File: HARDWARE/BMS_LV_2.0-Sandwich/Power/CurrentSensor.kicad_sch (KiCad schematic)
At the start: 7 parts, among them U5 ACHS-7123

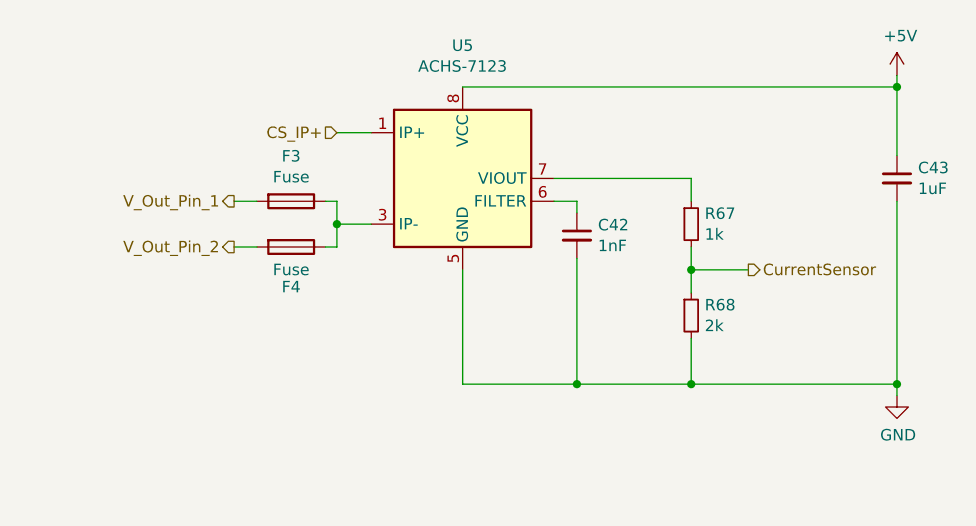
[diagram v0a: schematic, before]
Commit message: Zmieniono polozenie bezpiecznikow, dodano ledy sygnalizujące czy bezpiecznik jest cały
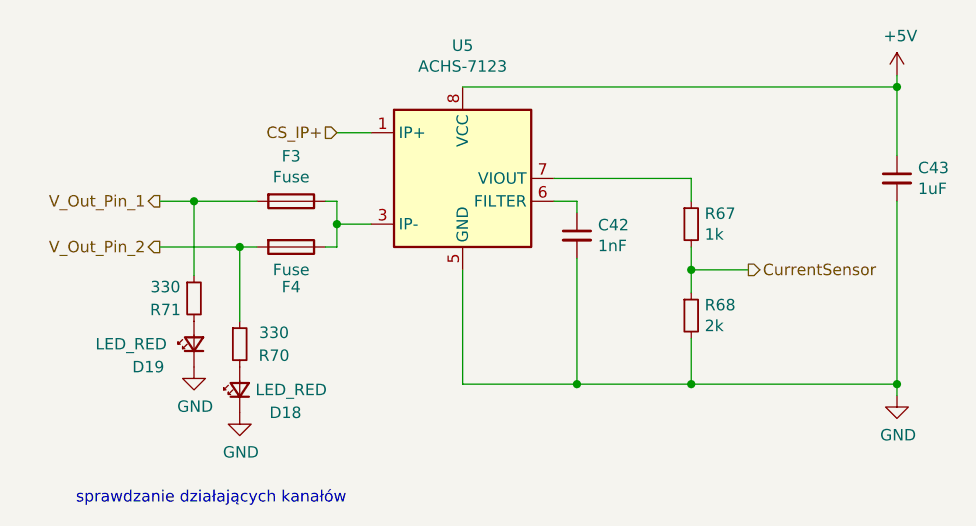
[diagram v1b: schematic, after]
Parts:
- added D18, D19: LED_RED, LED_SMD:LED_0603_1608Metric, symbol Device:LED_Small
- added R70, R71: 330, Resistor_SMD:R_0603_1608Metric, symbol Device:R_Small
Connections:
- net GND: now also D18.1 (K), D19.1 (K)
- net V_Out_Pin_1: now also R71.1
- net V_Out_Pin_2: now also R70.1
- new net: D19.2 (A), R71.2
- new net: D18.2 (A), R70.2
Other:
- note added: "sprawdzanie działających kanałów"

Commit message: sync
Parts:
- R70, R71: value 330 -> 1k5
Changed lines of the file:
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@@
 			)
 		)
-		(property "Value" "330"
+		(property "Value" "1k5"
 			(at 104.14 106.045 0)
 			(effects
@@
 			)
 		)
-		(property "Value" "330"
+		(property "Value" "1k5"
 			(at 116.205 111.125 0)
 			(effects

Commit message: Wersja obu plytek gotowa do sprawdzenia
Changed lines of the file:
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@@
+	)
+	(symbol
+		(lib_id "Device:Fuse")
+		(at 118.11 101.6 270)
+		(unit 1)
+		(exclude_from_sim no)
+		(in_bom yes)
+		(on_board yes)
+		(dnp no)
+		(property "Reference" "F4"
+			(at 118.11 96.5962 90)
+			(effects
+				(font
+					(size 1.27 1.27)
+				)
+			)
+		)
+		(property "Value" "Fuse"
+			(at 118.11 98.9076 90)
+			(effects
+				(font
+					(size 1.27 1.27)
+				)
+			)
+		)
+		(property "Footprint" "footprints:FUSC6125X279N"
+			(at 118.11 99.822 90)
+			(effects
+				(font
+					(size 1.27 1.27)
+				)
+				(hide yes)
+			)
+		)
+		(property "Datasheet" "https://www.mouser.pl/ProductDetail/Bel-Fuse/0680L9100-05?qs=XeJtXLiO41RjXNhvn3uPUw%3D%3D"
+			(at 118.11 101.6 0)
+			(effects
+				(font
+					(size 1.27 1.27)
+				)
+				(hide yes)
+			)
+		)
+		(property "Description" "500A interrupt fuse"
+			(at 118.11 101.6 0)
+			(effects
+				(font
+					(size 1.27 1.27)
+				)
+				(hide yes)
+			)
+		)
+		(property "Part Number" "0680L9100-05 "
+			(at 118.11 101.6 0)
+			(effects
+				(font
+					(size 1.27 1.27)
+				)
+				(hide yes)
+			)
+		)
+		(pin "2"
+		)
+		(pin "1"
+		)
+		(instances
+			(project "BMS_LV_2022"
+				(path "/fb6504b5-591d-4b10-ab86-0c46f59e8b7d/00000000-0000-0000-0000-000062c2dd72"
+					(reference "F4")
+					(unit 1)
+				)
+			)
+		)
 	)
 	(symbol
@@
 					(unit 1)
 				)
-			)
-		)
-	)
-	(symbol
-		(lib_id "Device:Fuse")
-		(at 118.11 101.6 270)
-		(unit 1)
-		(exclude_from_sim no)
-		(in_bom yes)
-		(on_board yes)
-		(dnp no)
-		(property "Reference" "F4"
-			(at 118.11 106.045 90)
-			(effects
-				(font
-					(size 1.27 1.27)
-				)
-			)
-		)
-		(property "Value" "Fuse"
-			(at 118.11 104.14 90)
-			(effects
-				(font
-					(size 1.27 1.27)
-				)
-			)
-		)
-		(property "Footprint" "footprints:FUSC6125X279N"
-			(at 118.11 99.822 90)
-			(effects
-				(font
-					(size 1.27 1.27)
-				)
-				(hide yes)
-			)
-		)
-		(property "Datasheet" "https://www.mouser.pl/ProductDetail/Bel-Fuse/0680L9100-05?qs=XeJtXLiO41RjXNhvn3uPUw%3D%3D"
-			(at 118.11 101.6 0)
-			(effects
-				(font
-					(size 1.27 1.27)
-				)
-				(hide yes)
-			)
-		)
-		(property "Description" "500A interrupt fuse"
-			(at 118.11 101.6 0)
-			(effects
-				(font
-					(size 1.27 1.27)
-				)
-				(hide yes)
-			)
-		)
-		(property "Part Number" "0680L9100-05 "
-			(at 118.11 101.6 0)
-			(effects
-				(font
-					(size 1.27 1.27)
-				)
-				(hide yes)
-			)
-		)
-		(pin "2"
-		)
-		(pin "1"
-		)
-		(instances
-			(project "BMS_LV_2022"
-				(path "/fb6504b5-591d-4b10-ab86-0c46f59e8b7d/00000000-0000-0000-0000-000062c2dd72"
-					(reference "F4")
-					(unit 1)
-				)

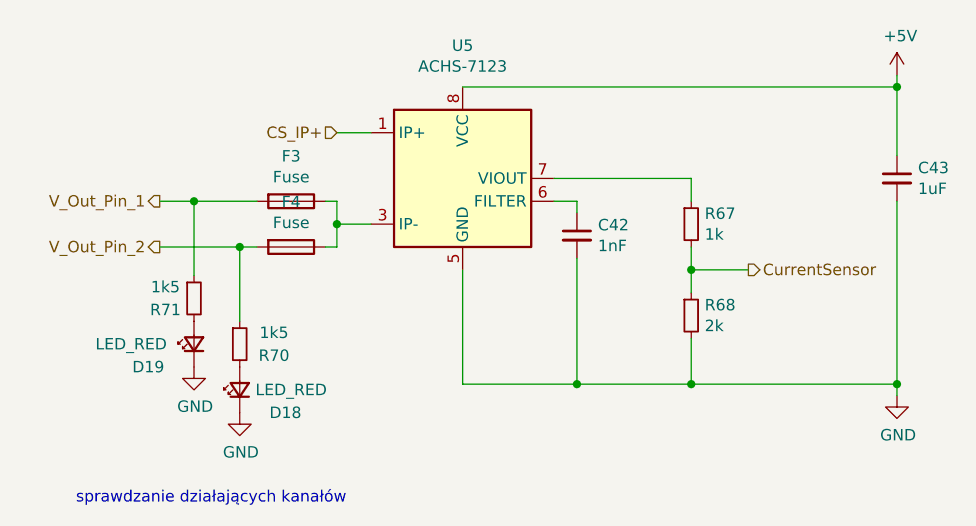
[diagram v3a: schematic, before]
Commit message: Zmiany w power: nowe bezpieczniki, nowy wymienialny layout dla tych bezpiecznikow, dodano diode zenera dla stabilizacji napięcia, zmiany dla control:  wyjebany eeprom, przesunięty can, zmieniony layout przetwornic, dodano programator i tvs, jeszcze do dokonczenia routing w control.
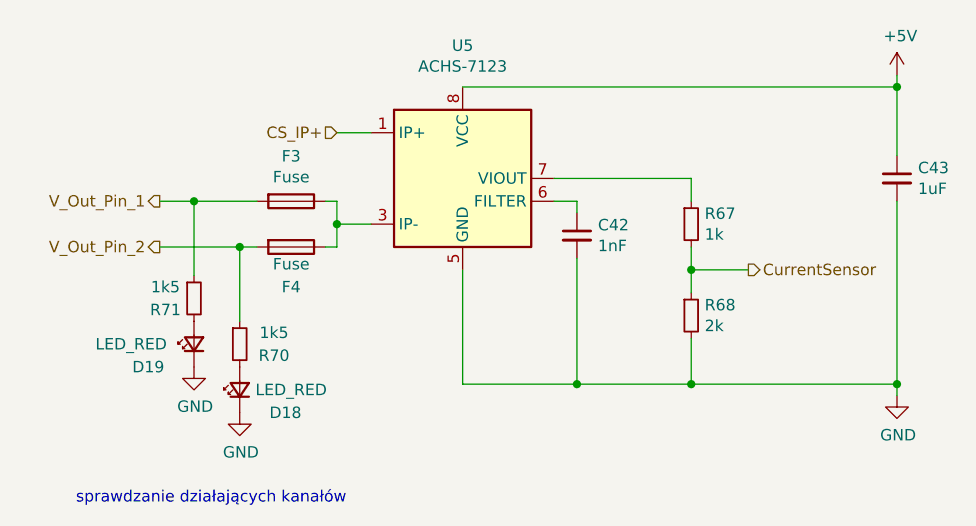
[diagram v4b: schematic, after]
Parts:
- F3, F4: footprint footprints:FUSC6125X279N -> footprints:01550900DR; Holder (none) -> https://www.mouser.co.il/ProductDetail/Littelfuse/01550900D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
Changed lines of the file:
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@@
 			)
 		)
-		(property "Footprint" "footprints:FUSC6125X279N"
+		(property "Footprint" "footprints:01550900DR"
 			(at 118.11 94.742 90)
 			(effects
@@
 			)
 		)
-		(property "Datasheet" "https://www.mouser.pl/ProductDetail/Bel-Fuse/0680L9100-05?qs=XeJtXLiO41RjXNhvn3uPUw%3D%3D"
+		(property "Datasheet" "https://eu.mouser.com/ProductDetail/Littelfuse/0451012.MRL?qs=vco6xy%252BeH1r0kN0Ehg8CxQ%3D%3D"
 			(at 118.11 96.52 0)
 			(effects
@@
 		(property "Part Number" "0680L9100-05 "
 			(at 118.11 96.52 0)
+			(effects
+				(font
+					(size 1.27 1.27)
+				)
+				(hide yes)
+			)
+		)
+		(property "Holder" "https://www.mouser.co.il/ProductDetail/Littelfuse/01550900DR?qs=DRkmTr78QATmF52QRk2Q4g%3D%3D"
+			(at 118.11 96.52 90)
 			(effects
 				(font
@@
 				(path "/fb6504b5-591d-4b10-ab86-0c46f59e8b7d/00000000-0000-0000-0000-000062c2dd72"
 					(reference "F3")
+					(unit 1)
+				)
+			)
+		)
+	)
+	(symbol
+		(lib_id "Device:Fuse")
+		(at 118.11 101.6 270)
+		(unit 1)
+		(exclude_from_sim no)
+		(in_bom yes)
+		(on_board yes)
+		(dnp no)
+		(property "Reference" "F4"
+			(at 118.11 106.045 90)
+			(effects
+				(font
+					(size 1.27 1.27)
+				)
+			)
+		)
+		(property "Value" "Fuse"
+			(at 118.11 103.505 90)
+			(effects
+				(font
+					(size 1.27 1.27)
+				)
+			)
+		)
+		(property "Footprint" "footprints:01550900DR"
+			(at 118.11 99.822 90)
+			(effects
+				(font
+					(size 1.27 1.27)
+				)
+				(hide yes)
+			)
+		)
+		(property "Datasheet" "https://eu.mouser.com/ProductDetail/Littelfuse/0451012.MRL?qs=vco6xy%252BeH1r0kN0Ehg8CxQ%3D%3D"
+			(at 118.11 101.6 0)
+			(effects
+				(font
+					(size 1.27 1.27)
+				)
+				(hide yes)
+			)
+		)
+		(property "Description" "500A interrupt fuse"
+			(at 118.11 101.6 0)
+			(effects
+				(font
+					(size 1.27 1.27)
+				)
+				(hide yes)
+			)
+		)
+		(property "Part Number" "0680L9100-05 "
+			(at 118.11 101.6 0)
+			(effects
+				(font
+					(size 1.27 1.27)
+				)
+				(hide yes)
+			)
+		)
+		(property "Holder" "https://www.mouser.co.il/ProductDetail/Littelfuse/01550900DR?qs=DRkmTr78QATmF52QRk2Q4g%3D%3D"
+			(at 118.11 101.6 90)
+			(effects
+				(font
+					(size 1.27 1.27)
+				)
+				(hide yes)
+			)
+		)
+		(pin "2"
+		)
+		(pin "1"
+		)
+		(instances
+			(project "BMS_LV_2022"
+				(path "/fb6504b5-591d-4b10-ab86-0c46f59e8b7d/00000000-0000-0000-0000-000062c2dd72"
+					(reference "F4")
 					(unit 1)
 				)
@@
 					(unit 1)
 				)
-			)
-		)
-	)
-	(symbol
-		(lib_id "Device:Fuse")
-		(at 118.11 101.6 270)
-		(unit 1)
-		(exclude_from_sim no)
-		(in_bom yes)
-		(on_board yes)
-		(dnp no)
-		(property "Reference" "F4"
-			(at 118.11 96.5962 90)
-			(effects
-				(font
-					(size 1.27 1.27)
-				)
-			)
-		)
-		(property "Value" "Fuse"
-			(at 118.11 98.9076 90)
-			(effects
-				(font
-					(size 1.27 1.27)
-				)
-			)
-		)
-		(property "Footprint" "footprints:FUSC6125X279N"
-			(at 118.11 99.822 90)
-			(effects
-				(font
-					(size 1.27 1.27)
-				)
-				(hide yes)
-			)
-		)
-		(property "Datasheet" "https://www.mouser.pl/ProductDetail/Bel-Fuse/0680L9100-05?qs=XeJtXLiO41RjXNhvn3uPUw%3D%3D"
-			(at 118.11 101.6 0)
-			(effects
-				(font
-					(size 1.27 1.27)
-				)
-				(hide yes)
-			)
-		)
-		(property "Description" "500A interrupt fuse"
-			(at 118.11 101.6 0)
-			(effects
-				(font
-					(size 1.27 1.27)
-				)
-				(hide yes)
-			)
-		)
-		(property "Part Number" "0680L9100-05 "
-			(at 118.11 101.6 0)
-			(effects
-				(font
-					(size 1.27 1.27)
-				)
-				(hide yes)
-			)
-		)
-		(pin "2"
-		)
-		(pin "1"
-		)
-		(instances
-			(project "BMS_LV_2022"
-				(path "/fb6504b5-591d-4b10-ab86-0c46f59e8b7d/00000000-0000-0000-0000-000062c2dd72"
-					(reference "F4")
-					(unit 1)
-				)

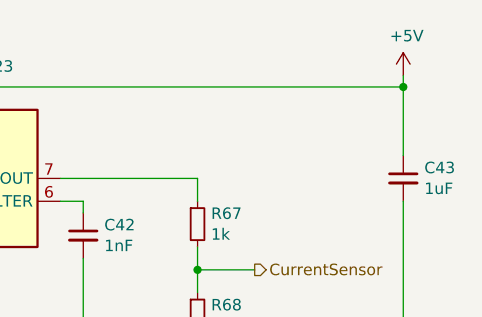
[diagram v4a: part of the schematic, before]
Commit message: Pierwsza wersja bez błędów DRC/ERC, skończony routing plytki control
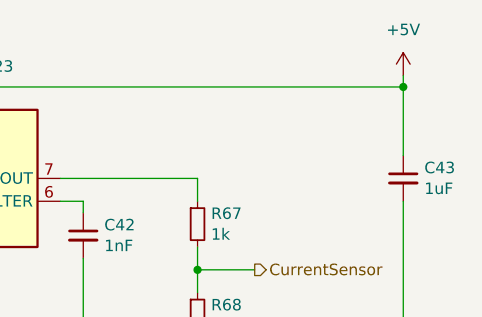
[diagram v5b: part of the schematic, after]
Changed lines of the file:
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@@
-	)
-	(symbol
-		(lib_id "BMS_LV_2022-rescue:+5V-power")
-		(at 185.42 82.55 0)
-		(unit 1)
-		(exclude_from_sim no)
-		(in_bom yes)
-		(on_board yes)
-		(dnp no)
-		(property "Reference" "#PWR049"
-			(at 185.42 86.36 0)
-			(effects
-				(font
-					(size 1.27 1.27)
-				)
-				(hide yes)
-			)
-		)
-		(property "Value" "+5V"
-			(at 185.801 78.1558 0)
-			(effects
-				(font
-					(size 1.27 1.27)
-				)
-			)
-		)
-		(property "Footprint" ""
-			(at 185.42 82.55 0)
-			(effects
-				(font
-					(size 1.27 1.27)
-				)
-				(hide yes)
-			)
-		)
-		(property "Datasheet" ""
-			(at 185.42 82.55 0)
-			(effects
-				(font
-					(size 1.27 1.27)
-				)
-				(hide yes)
-			)
-		)
-		(property "Description" ""
-			(at 185.42 82.55 0)
-			(effects
-				(font
-					(size 1.27 1.27)
-				)
-				(hide yes)
-			)
-		)
-		(pin "1"
-		)
-		(instances
-			(project "BMS_LV_2022"
-				(path "/fb6504b5-591d-4b10-ab86-0c46f59e8b7d/00000000-0000-0000-0000-000062c2dd72"
-					(reference "#PWR049")
-					(unit 1)
-				)
-			)
-		)
 	)
 	(symbol
@@
 					(unit 1)
 				)
+			)
+		)
+	)
+	(symbol
+		(lib_id "power:+5V")
+		(at 185.42 82.55 0)
+		(unit 1)
+		(exclude_from_sim no)
+		(in_bom yes)
+		(on_board yes)
+		(dnp no)
+		(fields_autoplaced yes)
+		(property "Reference" "#PWR02"
+			(at 185.42 86.36 0)
+			(effects
+				(font
+					(size 1.27 1.27)
+				)
+				(hide yes)
+			)
+		)
+		(property "Value" "+5V"
+			(at 185.42 77.47 0)
+			(effects
+				(font
+					(size 1.27 1.27)
+				)
+			)
+		)
+		(property "Footprint" ""
+			(at 185.42 82.55 0)
+			(effects
+				(font
+					(size 1.27 1.27)
+				)
+				(hide yes)
+			)
+		)
+		(property "Datasheet" ""
+			(at 185.42 82.55 0)
+			(effects
+				(font
+					(size 1.27 1.27)
+				)
+				(hide yes)
+			)
+		)
+		(property "Description" "Power symbol creates a global label with name \"+5V\""
+			(at 185.42 82.55 0)
+			(effects
+				(font
+					(size 1.27 1.27)
+				)
+				(hide yes)
+			)
+		)
+		(pin "1"
+		)
+		(instances
+			(project "BMS_LV_2022"
+				(path "/fb6504b5-591d-4b10-ab86-0c46f59e8b7d/00000000-0000-0000-0000-000062c2dd72"
+					(reference "#PWR02")
+					(unit 1)
+				)
